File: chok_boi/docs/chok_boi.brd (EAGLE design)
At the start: 372 x 192 mm, 90 parts, among them U1 MPU-6000, U2 DRV8835

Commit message: Design review fixes
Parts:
- moved LED1 5.78 mm to (5.99, 51.4)
- moved R_LED1 5.78 mm to (9.25, 51.4)
- moved LED2 4.90 mm to (5.99, 49.4)
- moved R_LED2 4.90 mm to (9.25, 49.4)
- moved R_LED3 4.11 mm to (9.25, 47.4)
- moved LED3 4.09 mm to (5.99, 47.4)
- moved C_NR 1.13 mm to (4.57, 24.2), turned to 270 degrees
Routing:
- net GND: track 98.0 -> 81.0 mm, vias 27 -> 32
- net LED1: track 53.4 -> 48.5 mm
- net LED2: track 52.4 -> 48.0 mm
- net A3.3V: track 123.9 -> 127.0 mm, vias 0 -> 2
- net LED3: track 51.1 -> 48.4 mm
- net BOOT0: track 65.0 -> 63.3 mm
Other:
- board size 372 x 192 mm -> 86 x 74 mm
- board text added: "2017-2018 Chok Boi Sahil Gandhi, Eric Tan, Jason Xu"
- board text added: "3.3V"
- board text added: "GND"
- board text added: "RESET"
- board text added: "RX"
- board text added: "SWCLK"
- board text added: "SWDIO"
- board text added: "TX"

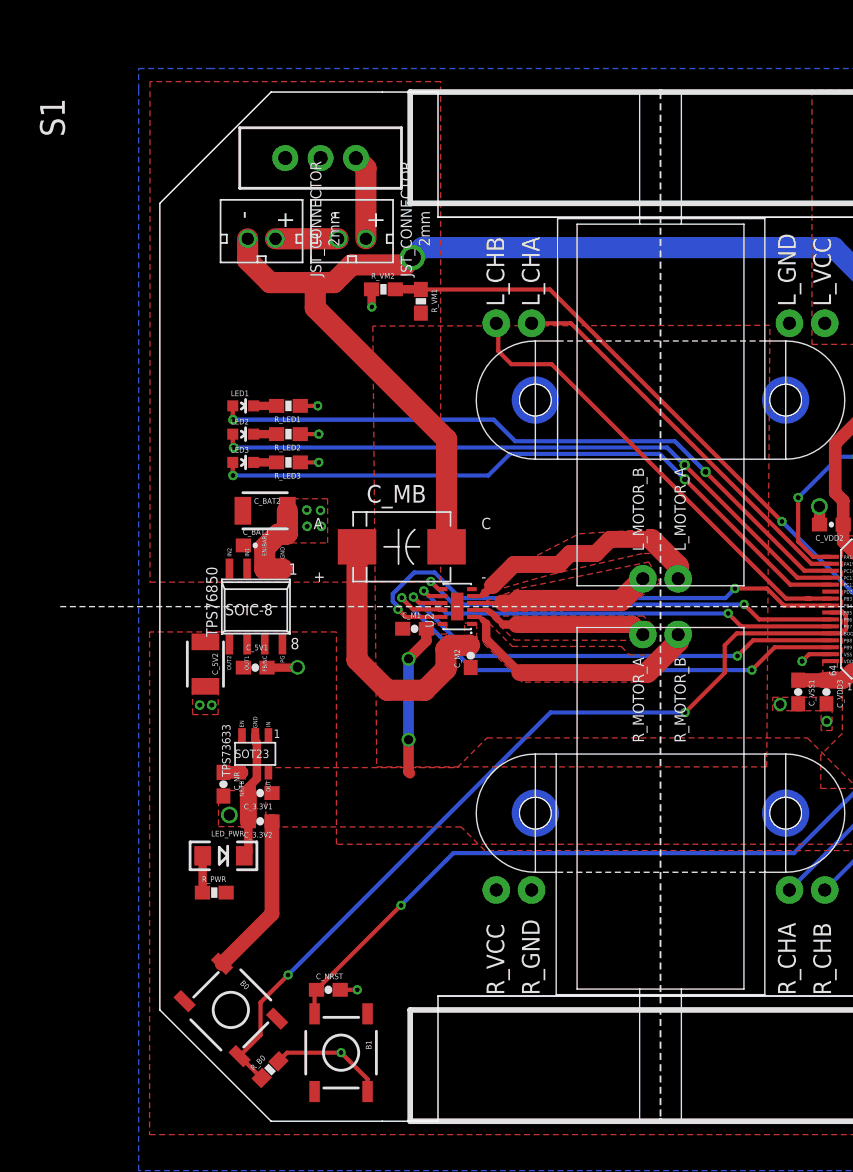
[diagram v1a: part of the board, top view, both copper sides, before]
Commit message: Add text to PCB and change values of 2 passives
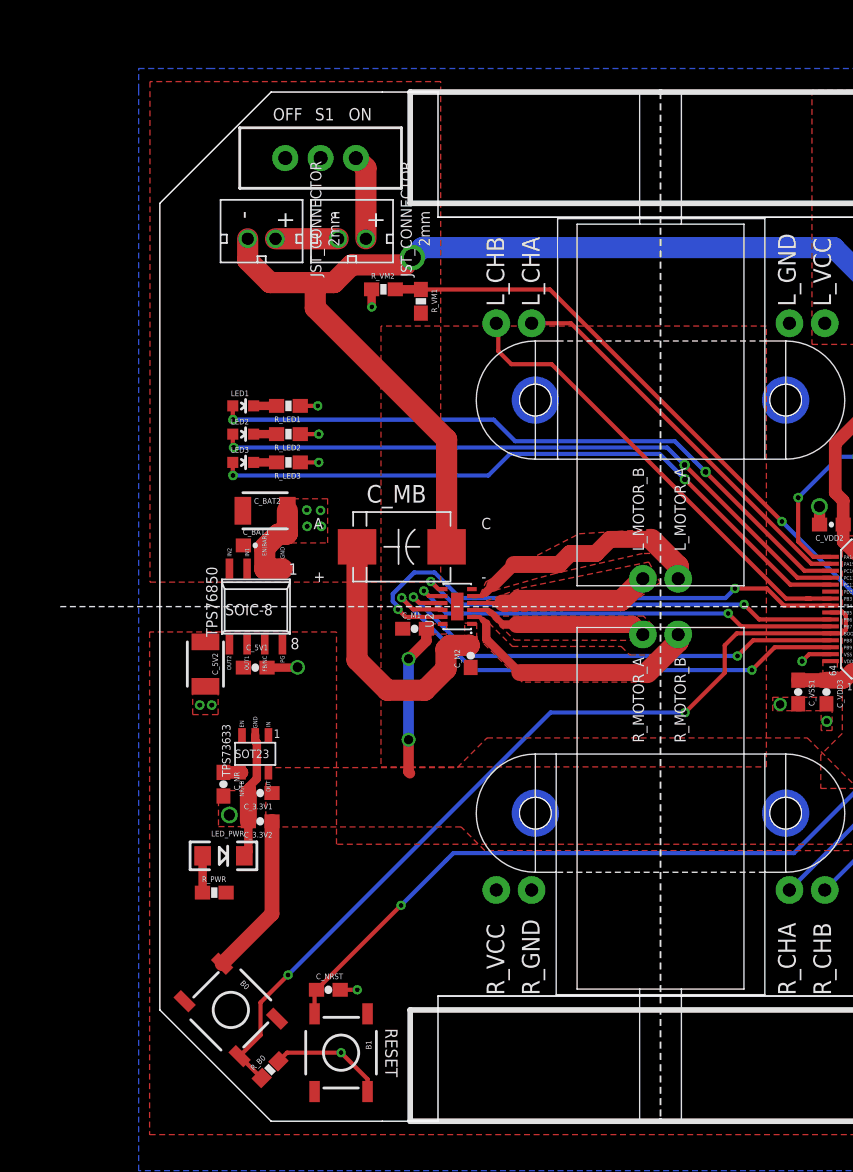
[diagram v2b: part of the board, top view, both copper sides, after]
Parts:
- C_GY_VDD: value 0.01uF -> 0.1uF
- R_VM1: value 20k -> 47k
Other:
- board text added: "OFF"
- board text added: "ON"
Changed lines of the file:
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@@
 <text x="56.8198" y="47.2948" size="0.508" layer="21">SWDIO</text>
 <text x="59.69" y="47.3202" size="0.508" layer="21">RESET</text>
+<text x="13.5636" y="71.9582" size="0.889" layer="21">ON</text>
+<text x="8.128" y="71.9582" size="0.889" layer="21">OFF</text>
+<text x="16.2052" y="6.6802" size="0.889" layer="21" rot="SR270">RESET</text>
 </plain>
 <attributes>
@@
 <attribute name="VALUE" x="5.842" y="31.4706" size="0.4064" layer="27" font="vector"/>
 </element>
-<element name="C_GY_VDD" library="SparkFun" package="0603-CAP" value="0.01uF" x="72.3646" y="37.0078" smashed="yes" rot="R90">
+<element name="C_GY_VDD" library="SparkFun" package="0603-CAP" value="0.1uF" x="72.3646" y="37.0078" smashed="yes" rot="R90">
 <attribute name="NAME" x="71.6026" y="36.1188" size="0.4064" layer="25" font="vector" rot="R90"/>
 <attribute name="VALUE" x="73.5076" y="35.9918" size="0.4064" layer="27" font="vector" rot="R90"/>
@@
 <element name="R_RLH" library="SparkFun-Passives" package="0603-RES" value="1.8k" x="67.8688" y="53.721"/>
 <element name="R_RRD" library="SparkFun-Passives" package="0603-RES" value="1.8k" x="77.2668" y="28.702"/>
-<element name="R_VM1" library="SparkFun-Passives" package="0603-RES" value="20k" x="18.7706" y="58.9534" rot="R270"/>
+<element name="R_VM1" library="SparkFun-Passives" package="0603-RES" value="47k" x="18.7706" y="58.9534" rot="R270"/>
 <element name="R_VM2" library="SparkFun-Passives" package="0603-RES" value="10k" x="16.0782" y="59.817"/>
 <element name="S1" library="SparkFun" package="SWITCH-SPDT" value="" x="11.5588" y="69.254" smashed="yes" rot="R90">
-<attribute name="NAME" x="-6.8308" y="70.778" size="1.778" layer="25" ratio="10" rot="R90"/>
+<attribute name="NAME" x="11.1506" y="71.9582" size="0.889" layer="25" ratio="10"/>
 <attribute name="VALUE" x="21.0838" y="65.444" size="1.778" layer="27" ratio="10" rot="R90"/>
 </element>
@@
 <vertex x="27.1526" y="39.0398"/>
 </polygon>
-<wire x1="23.9268" y1="38.5064" x2="25.4508" y2="40.0304" width="1.2192" layer="1"/>
+<wire x1="23.9268" y1="38.5064" x2="25.4508" y2="40.0304" width="0.9144" layer="1"/>
 <wire x1="28.702" y1="40.0304" x2="29.4894" y2="40.8178" width="1.2192" layer="1"/>
 <wire x1="29.4894" y1="40.8178" x2="31.3436" y2="40.8178" width="1.2192" layer="1"/>
@@
 <contactref element="C_MB" pad="C"/>
 <polygon width="0.1524" layer="1" thermals="no" rank="4">
-<vertex x="43.8658" y="57.2262"/>
-<vertex x="15.3162" y="57.1754"/>
-<vertex x="15.5956" y="25.4762"/>
-<vertex x="43.6372" y="25.4762"/>
+<vertex x="43.6118" y="57.1754"/>
+<vertex x="15.9004" y="57.1754"/>
+<vertex x="15.9004" y="25.4762"/>
+<vertex x="43.6118" y="25.4762"/>
 </polygon>
 <wire x1="11.176" y1="58.4708" x2="20.619" y2="49.0278" width="1.524" layer="1"/>
